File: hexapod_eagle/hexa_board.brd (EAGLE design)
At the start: 80 x 90 mm, 52 parts

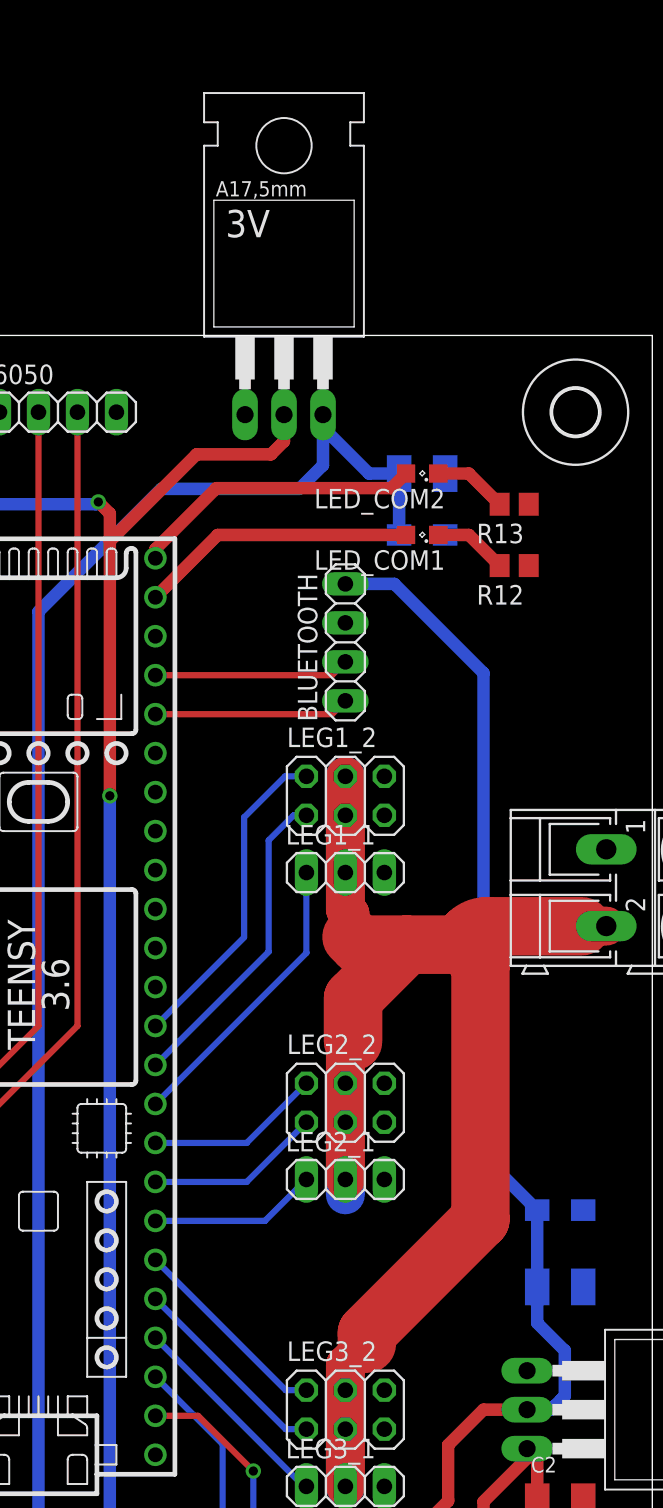
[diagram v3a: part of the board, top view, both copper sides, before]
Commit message: Update eagle board
-added sharp sensor
-some minor changes
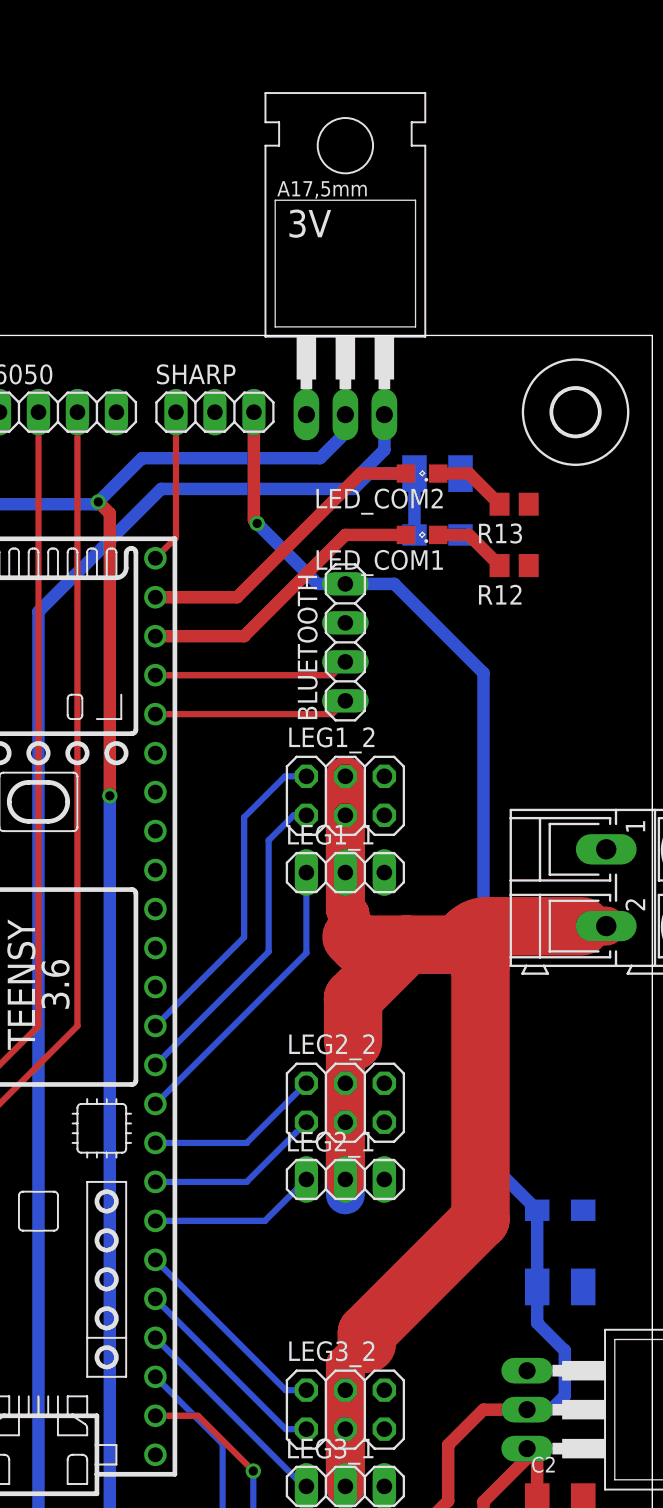
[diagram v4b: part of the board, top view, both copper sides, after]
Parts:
- added SHARP: (no value), pinhead:1X03
- moved 3V 4.00 mm to (20.0, 50.0)
- moved C7 1.00 mm to (26.0, 36.0)
- moved C9 1.00 mm to (26.0, 32.0)
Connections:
- new net SENSOR: SHARP.1, TEENSY41.32/A13
- net +5V: now also SHARP.3
- net GND: now also SHARP.2
- net LED1: now also TEENSY41.30; no longer TEENSY41.31/A12
- net LED2: now also TEENSY41.31/A12; no longer TEENSY41.32/A13
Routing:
- net +5V: track 110.6 -> 125.3 mm, vias 0 -> 1
- net SENSOR: track 0.00 -> 10.1 mm
- net +3V3: track 133.0 -> 136.4 mm
- net +BAT: track 162.5 -> 164.6 mm
- net LED1: track 18.0 -> 19.1 mm
- net LED2: track 19.0 -> 19.7 mm
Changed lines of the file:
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@@
 <elements>
 <element name="C10" library="rcl" package="SMC_A" value="100n" x="-8" y="35.5" rot="MR90"/>
-<element name="C7" library="rcl" package="SMC_B" value="10uF" x="25" y="36" rot="MR180"/>
+<element name="C7" library="rcl" package="SMC_B" value="10uF" x="26" y="36" rot="MR180"/>
 <element name="C8" library="rcl" package="SMC_B" value="10uF" x="-5" y="35.5" rot="MR90"/>
-<element name="C9" library="rcl" package="SMC_A" value="100n" x="25" y="32" rot="MR180"/>
+<element name="C9" library="rcl" package="SMC_A" value="100n" x="26" y="32" rot="MR180"/>
 <element name="LED_ZASILANIE" library="led" package="SML0805" value="" x="-15.85" y="35.99" rot="R270"/>
 <element name="LEG1_1" library="pinhead" package="1X03" value="" x="20" y="10"/>
@@
 <element name="R11" library="rcl" package="R0805" value="510r" x="-15" y="-27" rot="MR180"/>
 <element name="5V" library="mc33269" package="TO220" value="MC33269" x="42" y="-25" rot="R270"/>
-<element name="3V" library="mc33269" package="TO220" value="MC33269" x="16" y="50"/>
+<element name="3V" library="mc33269" package="TO220" value="MC33269" x="20" y="50"/>
 <element name="R12" library="rcl" package="R0805" value="510r" x="31" y="30" rot="R180"/>
 <element name="R13" library="rcl" package="R0805" value="510r" x="31" y="34" rot="R180"/>
 <element name="LED_COM1" library="led" package="SML0805" value="" x="25" y="32" rot="R180"/>
 <element name="LED_COM2" library="led" package="SML0805" value="" x="25" y="36" rot="R180"/>
+<element name="SHARP" library="pinhead" package="1X03" value="" x="11.5" y="40"/>
 </elements>
 <signals>
@@
 <wire x1="4.65" y1="-33.3" x2="4.65" y2="15" width="0.8128" layer="16"/>
 <via x="4.65" y="15" extent="1-16" drill="0.6" shape="square"/>
-<wire x1="4.65" y1="15" x2="4.65" y2="31.6" width="0.8128" layer="1"/>
-<wire x1="4.65" y1="31.6" x2="4.65" y2="33.4" width="0.8128" layer="1"/>
-<wire x1="16" y1="39.84" x2="16" y2="38.1" width="0.8128" layer="1"/>
-<wire x1="16" y1="38.1" x2="15.15" y2="37.25" width="0.8128" layer="1"/>
+<wire x1="4.65" y1="15" x2="4.65" y2="33.4" width="0.8128" layer="1"/>
 <wire x1="-5" y1="34" x2="3.75" y2="34" width="0.8128" layer="16"/>
 <wire x1="3.75" y1="34" x2="3.9" y2="34.15" width="0.8128" layer="16"/>
 <via x="3.9" y="34.15" extent="1-16" drill="0.6" shape="square"/>
 <wire x1="3.9" y1="34.15" x2="4.65" y2="33.4" width="0.8128" layer="1"/>
-<wire x1="4.65" y1="31.6" x2="10.3" y2="37.25" width="0.8128" layer="1"/>
-<wire x1="10.3" y1="37.25" x2="15.15" y2="37.25" width="0.8128" layer="1"/>
+<wire x1="20" y1="39.84" x2="20" y2="38.65" width="0.8128" layer="16"/>
+<wire x1="20" y1="38.65" x2="18.35" y2="37" width="0.8128" layer="16"/>
+<wire x1="18.35" y1="37" x2="6.75" y2="37" width="0.8128" layer="16"/>
+<wire x1="6.75" y1="37" x2="3.9" y2="34.15" width="0.8128" layer="16"/>
 </signal>
 <signal name="GND">
@@
 <contactref element="3V" pad="1"/>
 <contactref element="5V" pad="1"/>
+<contactref element="SHARP" pad="2"/>
 </signal>
 <signal name="INT">
@@
 <wire x1="5.9" y1="-36.1" x2="1" y2="-41" width="0.8128" layer="1"/>
 <contactref element="3V" pad="3"/>
-<wire x1="18.54" y1="39.84" x2="18.54" y2="39" width="0.8128" layer="16"/>
-<wire x1="18.54" y1="39" x2="18.54" y2="36.54" width="0.8128" layer="16"/>
-<wire x1="18.54" y1="36.54" x2="17" y2="35" width="0.8128" layer="16"/>
-<wire x1="17" y1="35" x2="8" y2="35" width="0.8128" layer="16"/>
+<wire x1="20.54" y1="35" x2="20" y2="35" width="0.8128" layer="16"/>
+<wire x1="20" y1="35" x2="8" y2="35" width="0.8128" layer="16"/>
 <wire x1="8" y1="35" x2="0" y2="27" width="0.8128" layer="16"/>
 <wire x1="0" y1="27" x2="0" y2="-40" width="0.8128" layer="16"/>
 <wire x1="0" y1="-40" x2="1" y2="-41" width="0.8128" layer="16"/>
 <wire x1="1" y1="-41" x2="1" y2="-41.7" width="0.8128" layer="16"/>
-<wire x1="23.5" y1="36" x2="21.54" y2="36" width="0.8128" layer="16"/>
-<wire x1="21.54" y1="36" x2="18.54" y2="39" width="0.8128" layer="16"/>
-<wire x1="23.5" y1="36" x2="23.5" y2="32" width="0.8128" layer="16"/>
+<wire x1="24.5" y1="36" x2="21.54" y2="36" width="0.8128" layer="16"/>
+<wire x1="24.5" y1="36" x2="24.5" y2="32" width="0.8128" layer="16"/>
 <wire x1="1" y1="-40.6146" x2="-6.6146" y2="-33" width="0.4064" layer="1"/>
 <wire x1="-6.6146" y1="-33" x2="-7.05" y2="-33" width="0.4064" layer="1"/>
@@
 <wire x1="32.5" y1="-28.2" x2="31.84" y2="-27.54" width="0.8128" layer="1"/>
 <wire x1="32.5" y1="-31" x2="32.5" y2="-34" width="0.8128" layer="1"/>
+<wire x1="20.54" y1="35" x2="21.54" y2="36" width="0.8128" layer="16"/>
+<wire x1="22.54" y1="39.84" x2="22.54" y2="37.54" width="0.8128" layer="16"/>
+<wire x1="22.54" y1="37.54" x2="20" y2="35" width="0.8128" layer="16"/>
 </signal>
 <signal name="+5V">
@@
 <wire x1="-2.51" y1="-33.05" x2="-7.62" y2="-27.94" width="0.8128" layer="1"/>
 <wire x1="29" y1="-8.5" x2="29" y2="23" width="0.8128" layer="16"/>
-<wire x1="20" y1="28.81" x2="23.19" y2="28.81" width="0.8128" layer="16"/>
+<wire x1="20" y1="28.81" x2="21" y2="28.81" width="0.8128" layer="16"/>
+<wire x1="21" y1="28.81" x2="23.19" y2="28.81" width="0.8128" layer="16"/>
 <wire x1="29" y1="23" x2="23.19" y2="28.81" width="0.8128" layer="16"/>
 <contactref element="5V" pad="2"/>
@@
 <wire x1="32.5" y1="-12" x2="32.5" y2="-17" width="0.8128" layer="16"/>
 <wire x1="31.84" y1="-25" x2="33.4" y2="-25" width="0.8128" layer="16"/>
-<wire x1="33.4" y1="-25" x2="33.7" y2="-24.7" width="0.8128" layer="16"/>
-<wire x1="33.7" y1="-24.7" x2="34.05" y2="-24.35" width="0.8128" layer="16"/>
+<wire x1="33.4" y1="-25" x2="34.3" y2="-24.1" width="0.8128" layer="16"/>
 <wire x1="32.5" y1="-17" x2="32.5" y2="-19.35" width="0.8128" layer="16"/>
 <wire x1="32.5" y1="-19.35" x2="34.3" y2="-21.15" width="0.8128" layer="16"/>
 <wire x1="34.3" y1="-21.15" x2="34.3" y2="-24.1" width="0.8128" layer="16"/>
-<wire x1="34.3" y1="-24.1" x2="34.05" y2="-24.35" width="0.8128" layer="16"/>
+<contactref element="SHARP" pad="3"/>
+<wire x1="14.04" y1="40" x2="14.04" y2="32.96" width="0.8128" layer="1"/>
+<wire x1="14.04" y1="32.96" x2="14.25" y2="32.75" width="0.8128" layer="1"/>
+<via x="14.25" y="32.75" extent="1-16" drill="0.6" shape="square"/>
+<wire x1="14.25" y1="32.75" x2="18.19" y2="28.81" width="0.8128" layer="16"/>
+<wire x1="18.19" y1="28.81" x2="20" y2="28.81" width="0.8128" layer="16"/>
 </signal>
 <signal name="RXD">
@@
 <signal name="LED1">
 <contactref element="LED_COM1" pad="A"/>
-<contactref element="TEENSY41" pad="31/A12"/>
-<wire x1="23.95" y1="32" x2="11.68" y2="32" width="0.8128" layer="1"/>
-<wire x1="11.68" y1="32" x2="7.62" y2="27.94" width="0.8128" layer="1"/>
+<contactref element="TEENSY41" pad="30"/>
+<wire x1="7.62" y1="25.4" x2="13.4" y2="25.4" width="0.8128" layer="1"/>
+<wire x1="23.95" y1="32" x2="20" y2="32" width="0.8128" layer="1"/>
+<wire x1="20" y1="32" x2="13.4" y2="25.4" width="0.8128" layer="1"/>
 </signal>
 <signal name="LED2">
 <contactref element="LED_COM2" pad="A"/>
+<contactref element="TEENSY41" pad="31/A12"/>
+<wire x1="7.62" y1="27.94" x2="12.94" y2="27.94" width="0.8128" layer="1"/>
+<wire x1="23.95" y1="36" x2="21" y2="36" width="0.8128" layer="1"/>
+<wire x1="21" y1="36" x2="12.94" y2="27.94" width="0.8128" layer="1"/>
+</signal>
+<signal name="SENSOR">
 <contactref element="TEENSY41" pad="32/A13"/>
-<wire x1="7.62" y1="30.48" x2="7.62" y2="31.07" width="0.8128" layer="1"/>
-<wire x1="7.62" y1="31.07" x2="11.6" y2="35.05" width="0.8128" layer="1"/>
-<wire x1="11.6" y1="35.05" x2="23" y2="35.05" width="0.8128" layer="1"/>
-<wire x1="23" y1="35.05" x2="23.95" y2="36" width="0.8128" layer="1"/>
+<contactref element="SHARP" pad="1"/>
+<wire x1="8.96" y1="40" x2="8.96" y2="31.82" width="0.4064" layer="1"/>
+<wire x1="8.96" y1="31.82" x2="7.62" y2="30.48" width="0.4064" layer="1"/>
 </signal>
 </signals>
